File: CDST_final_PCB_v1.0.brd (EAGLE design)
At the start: 160 x 100 mm, 39 parts, among them IC1 MIC_I2S_SPH0645, U1 AD8232ACPZ-R7

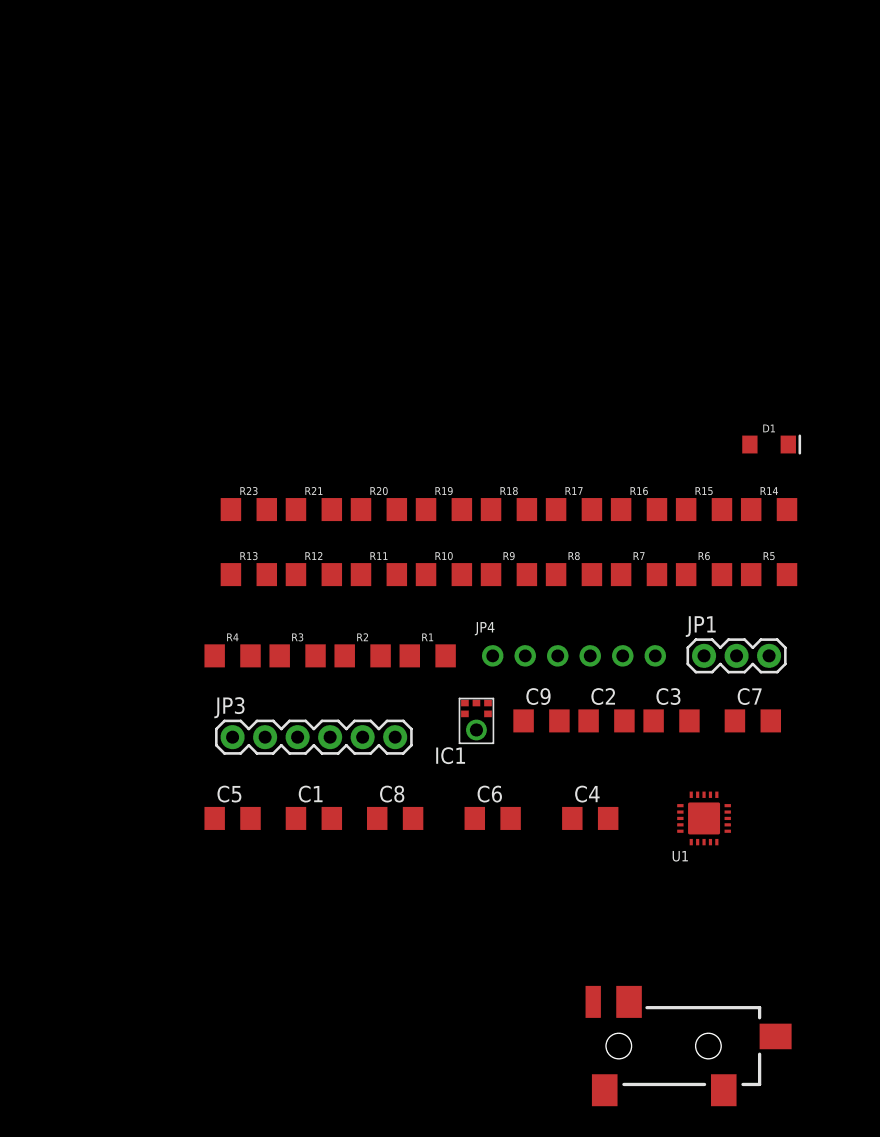
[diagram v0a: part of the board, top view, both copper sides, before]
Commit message: added power electronics
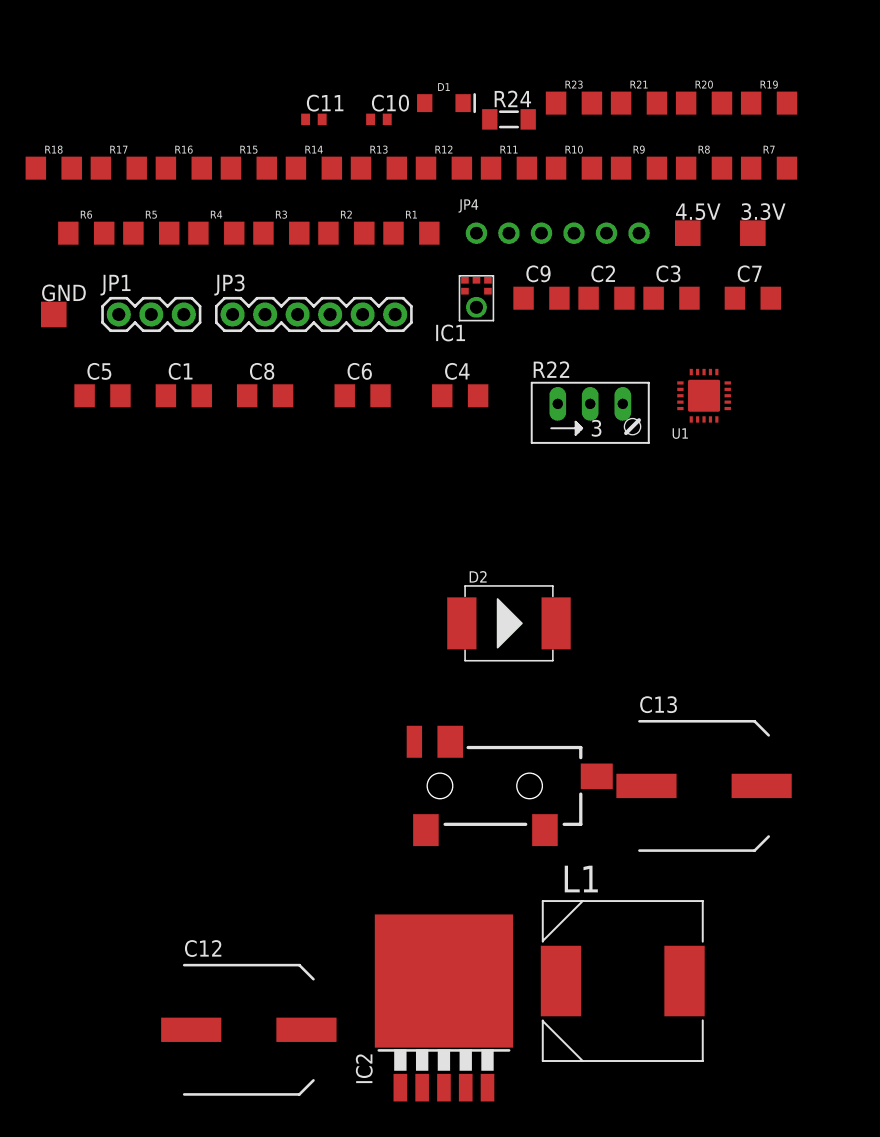
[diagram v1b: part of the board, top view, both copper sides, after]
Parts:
- added 3.3V, 4.5V, GND: TPTP20SQ, testpad:TP20SQ
- added C10, C11: (no value), rcl:C0402
- added C12, C13: (no value), rcl:SANYO-OSCON_SMD_F8
- added D2: SMD-DIODE-SCHOTTKY-40V-3A(DO-214AB), SMD-DIODE-SCHOTTKY-40V-3A_DO-214AB_:DO-214AB
- added IC2: LM2596S, national-semiconductor:TO263-5
- added L1: DR125-471-R, DR125-471-R:INDM125125X600N
- added R22: (no value), pot:RJ9W
- added R24: (no value), rcl:MINI_MELF-0204W
- moved R5 55.1 mm to (-63.5, 68.6)
- moved R6 55.1 mm to (-68.6, 68.6)
- moved JP1 52.9 mm to (-66.0, 62.2)
- moved R14 44.4 mm to (-50.8, 73.7)
- moved R15 44.4 mm to (-55.9, 73.7)
- moved R16 44.4 mm to (-61.0, 73.7)
- moved R17 44.4 mm to (-66.0, 73.7)
- moved R18 44.4 mm to (-71.1, 73.7)
- moved R23 40.7 mm to (-30.5, 78.7)
- moved R19 40.7 mm to (-15.2, 78.7)
- moved R20 40.7 mm to (-20.3, 78.7)
- moved R21 40.7 mm to (-25.4, 78.7)
- moved D1 36.8 mm to (-40.6, 78.7)
- moved C1 34.5 mm to (-61.0, 55.9)
- moved C5 34.5 mm to (-67.3, 55.9)
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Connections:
- new net N$12: C10.1, IC2.4, R22.E, R22.S, R24.2
- new net N$21: D2.2, IC2.2, L1.2
- new net N$6: 4.5V.TP, C11.1, C12.+, IC2.1
- new net V_REG: 3.3V.TP, C10.2, C13.+, C8.2, C9.2, JP4.1, L1.1, R17.1, R22.A
- net GND: now also C11.2, C12.-, C13.-, D2.1, GND.TP, IC2.3, IC2.5, R24.1
- net VCC: no longer R17.1
- net VDD: no longer C8.2, C9.2, JP4.1

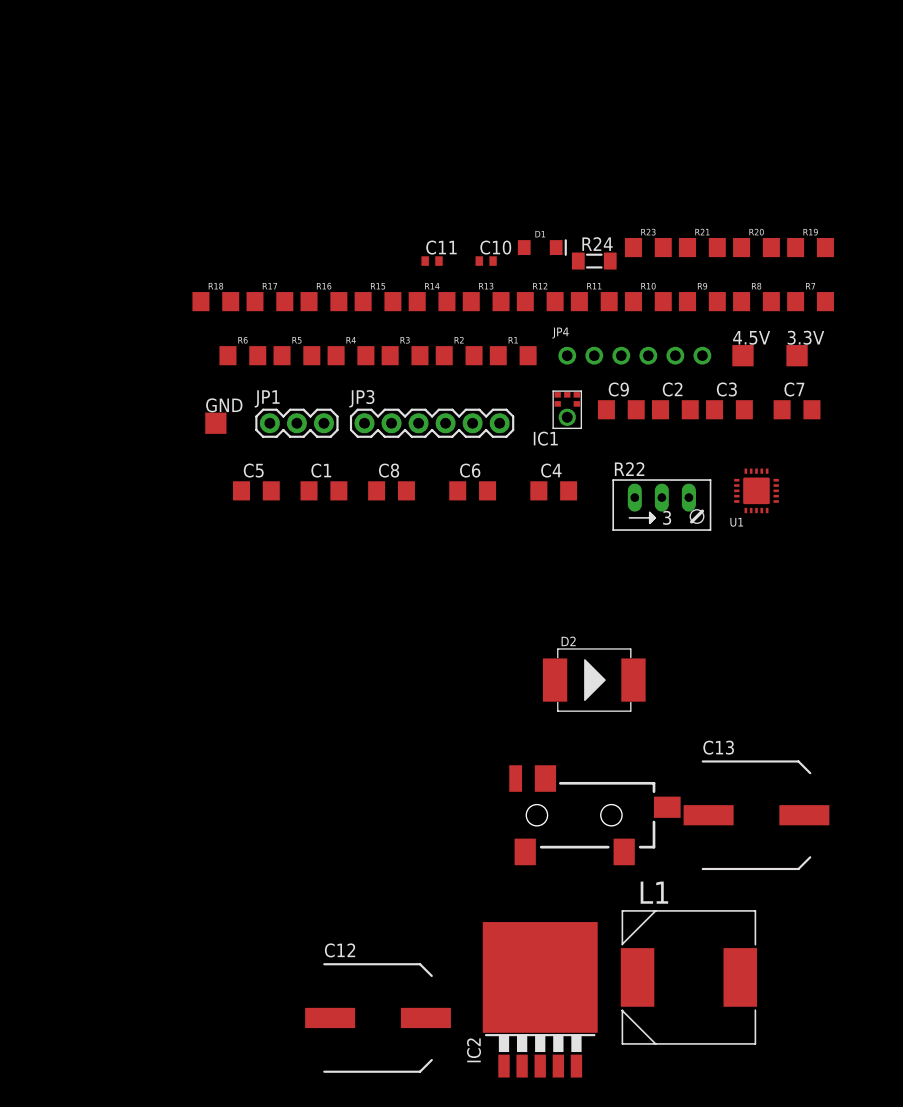
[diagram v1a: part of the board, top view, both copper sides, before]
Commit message: added esp32
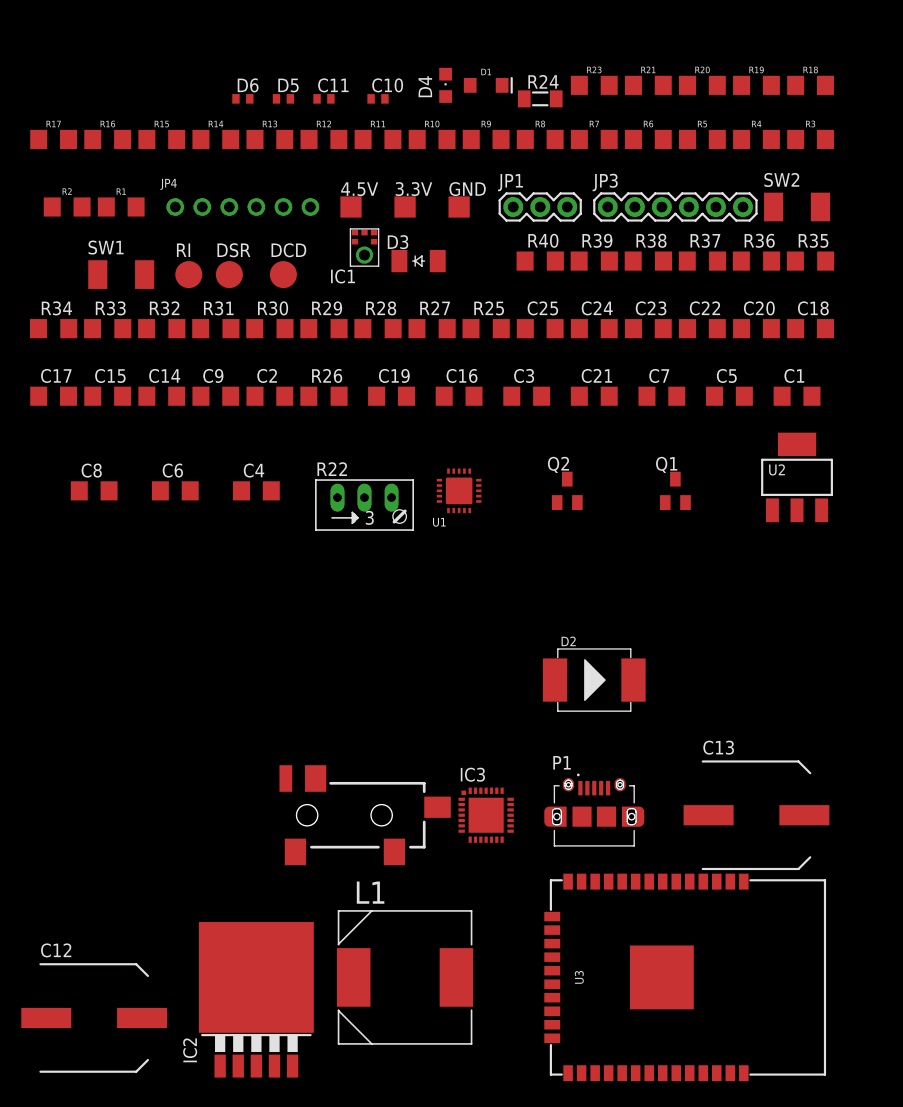
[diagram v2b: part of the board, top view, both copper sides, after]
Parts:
- added C14, C18, C20, C23: 10u, eagle-ltspice:C1206
- added C15: 22u, eagle-ltspice:C1206
- added C16, C19: 0.1u, eagle-ltspice:C1206
- added C17, C24, C25: 1n, eagle-ltspice:C1206
- added C21: 100u, eagle-ltspice:C1206
- added C22: 1u, eagle-ltspice:C1206
- added D3: CGRM4001-G, diode:SOD-123_MINI-SMA
- added D4: (no value), led:CHIPLED_0805
- added D5, D6: (no value), eagle-ltspice:R0402
- added DCD, DSR, RI: TPB2,54, testpad:B2,54
- added IC3: CP2101, silabs:MLP28
- added P1: ZX62D-B-5P8, ZX62D-B-5P8:HRS_ZX62D-B-5P8
- added Q1, Q2: BCX70SMD, transistor:SOT23
- added R25: 2k, eagle-ltspice:R1206
- added R26: 3.3k, eagle-ltspice:R1206
- added R27, R34, R35, R36, R37, R40: 0, eagle-ltspice:R1206
- added R28, R30, R31: 12k, eagle-ltspice:R1206
- added R29, R32, R33: 470, eagle-ltspice:R1206
- added R38, R39: 5k, eagle-ltspice:R1206
- added SW1, SW2: (no value), eagle-ltspice:R2010
- added U2: (no value), bt_regulator:SOT-223-3
- added U3: ESP-WROOM-03, esp32:ESP-WROOM-03
- moved R18 59.5 mm to (-15.2, 94.0)
- moved C1 45.3 mm to (-16.5, 64.8)
- moved C5 45.3 mm to (-22.9, 64.8)
- moved R3 43.2 mm to (-15.2, 88.9)
- moved R4 43.2 mm to (-20.3, 88.9)
- moved R5 43.2 mm to (-25.4, 88.9)
- moved R6 43.2 mm to (-30.5, 88.9)
- moved R1 39.4 mm to (-80.0, 82.5)
- moved R2 39.4 mm to (-85.1, 82.5)
- moved 3.3V 39.4 mm to (-53.3, 82.5)
- moved 4.5V 39.4 mm to (-58.4, 82.5)
- moved JP4 39.4 mm to (-68.6, 82.5)
- moved C2 38.1 mm to (-66.0, 64.8)
- moved C9 38.1 mm to (-71.1, 64.8)
- moved GND 30.6 mm to (-48.3, 82.5)
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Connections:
- removed net 3.3V: JP3.2, R15.2
- removed net VCC: C5.2, R10.1, R20.1, U1.15, U1.17
- removed net VDD: IC1.5
- new net DCD: DCD.TP, IC3.1
- new net HEATSINK: R40.2, U2.4
- new net N$20: C14.1, C16.1, C18.1, D3.C, IC3.8, R25.2, U2.3
- new net N$23: D5.2, IC3.4, P1.3
- new net N$24: D6.2, IC3.5, P1.2
- new net N$25: D3.A, P1.1
- new net N$26: Q1.1, R28.2
- new net N$27: IC3.24, Q1.2, R30.1, R36.2
- new net N$28: IC3.28, Q2.2, R28.1
- new net N$29: C24.1, Q1.3, R31.2, R33.2, U3.3
- new net N$30: IC3.25, R34.2
- new net N$31: IC3.26, R29.1
- new net N$33: U3.32, U3.37
- new net N$34: C25.1, R33.1, SW2.2
- new net N$35: C17.1, R32.1, SW1.2
- new net N$36: Q2.3, R32.2, R39.1, U3.25
- new net N$37: R38.2, U3.24
- new net N$38: R34.1, U3.35
- new net N$39: R29.2, R35.2
- new net N$40: R35.1, U3.34
- new net N$41: R36.1, U3.16
- new net N$42: IC3.23, R37.2
- new net N$43: R37.1, U3.23
- new net N$44: Q2.1, R30.2
- new net N$45: IC3.2, RI.TP
- new net N$46: DSR.TP, IC3.27
- net GND: now also C14.2, C15.2, C16.2, C17.2, C18.2, C19.2, C20.2, C21.2, C22.2, C23.1, C23.2, C24.2, C25.2, D4.C, D5.1, D6.1, IC3.3, IC3.EXP, IC3.M, P1.5, R26.1, R27.1, R27.2, R38.1, SW1.1, SW2.1, U2.1, U3.1, U3.15, U3.38, U3.GND
- net N$9: now also D4.A, R25.1; no longer C3.2, R8.2, U1.8
- net REFOUT: now also C3.2, R8.2, U1.8
- net V_REG: now also C15.1, C19.1, C20.1, C21.1, C22.1, C5.2, IC1.5, IC3.6, IC3.7, JP3.2, R10.1, R15.2, R20.1, R26.2, R31.1, R39.2, R40.1, U1.15, U1.17, U2.2, U3.2

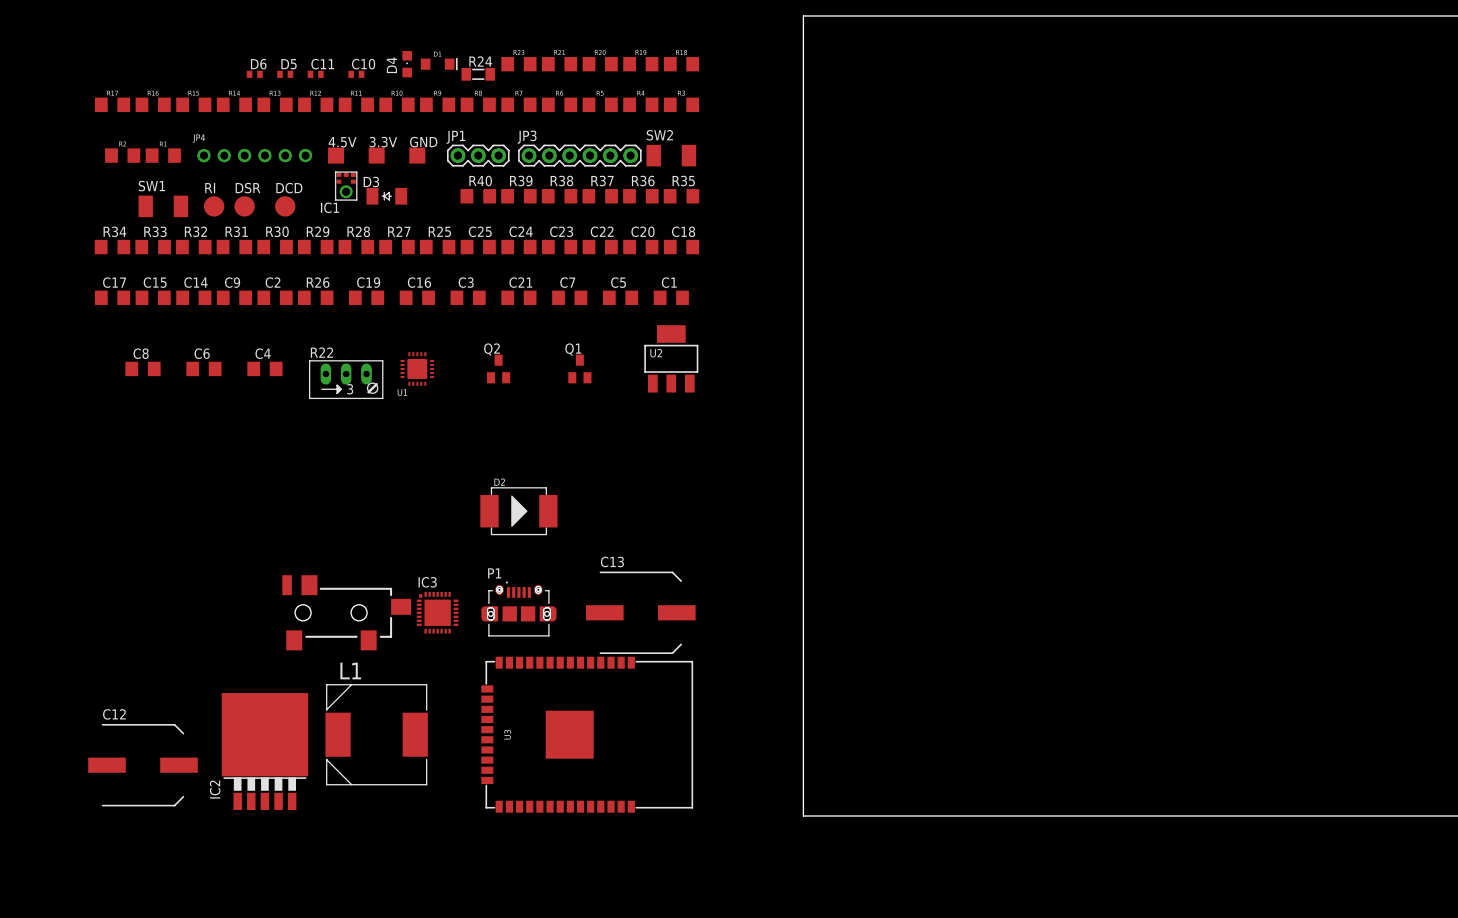
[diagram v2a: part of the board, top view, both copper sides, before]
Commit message: Test pin added to ESP
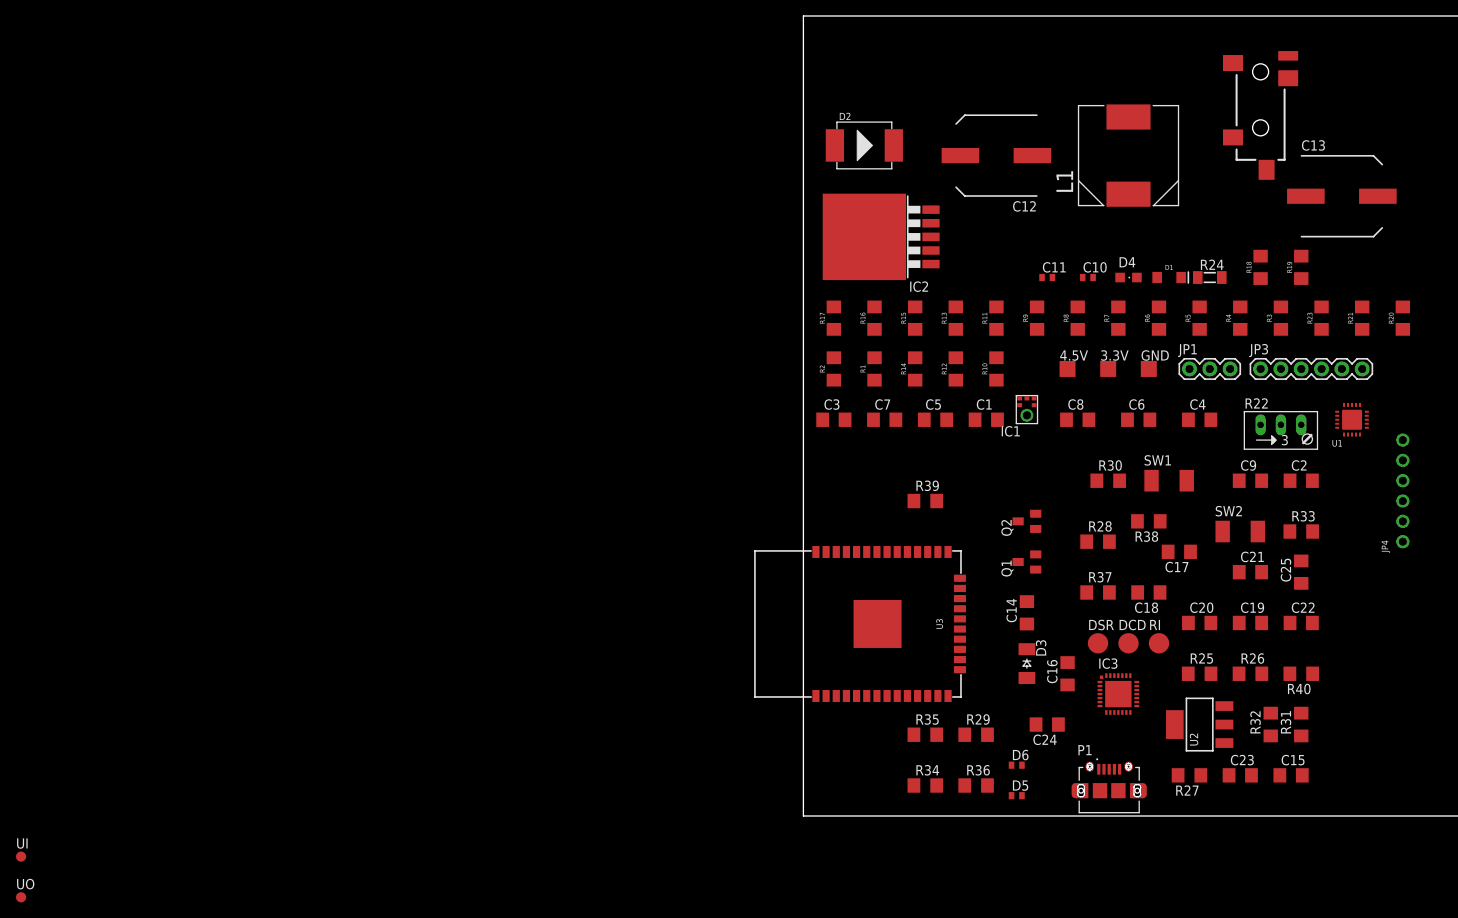
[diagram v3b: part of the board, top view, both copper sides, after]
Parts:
- added UI, UO: TPB1,27, testpad:B1,27
- moved C15 154.3 mm to (61.0, 5.08)
- moved JP4 149.5 mm to (74.9, 40.6), turned to 90 degrees
- moved R33 147.9 mm to (62.2, 35.6)
- moved R32 147.3 mm to (58.4, 11.4), turned to 90 degrees
- moved R31 146.1 mm to (62.2, 11.4), turned to 90 degrees
- moved JP2 142.2 mm to (57.1, 96.5), turned to 270 degrees
- moved C17 137.1 mm to (47.0, 33.0), turned to 180 degrees
- moved C12 131.1 mm to (24.1, 82.5), turned to 180 degrees
- moved SW1 130.3 mm to (45.7, 41.9)
- moved C2 130.3 mm to (62.2, 41.9)
- moved RI 130.1 mm to (44.5, 21.6)
- moved C9 129.0 mm to (55.9, 41.9)
- moved D6 128.6 mm to (26.7, 6.35)
- moved D5 128.4 mm to (26.7, 2.54)
- moved R26 125.9 mm to (55.9, 17.8)
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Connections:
- new net N$32: U3.13, UO.TP
- net BCLK: now also U3.11
- net DATA: now also R36.1, U3.16
- net GND: now also JP4.6
- net N$41: now also U3.14, UI.TP; no longer R36.1, U3.16
- net SELECT: no longer JP4.6
- net SIGNAL_OUT: now also U3.6
- net WS: now also U3.10

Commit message: layout revision v0.1
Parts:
- added D7: RED, SparkFun-LED:LED-1206
- added R41: 10k, SparkFun-Resistors:1206
- added S1: (no value), SparkFun-Switches:SWITCH_SPST_SMD_A
- added U4: 74LVC1G08SE, SparkFun-IC-Logic:SOT23-5
- moved UI 117.5 mm to (19.1, 7.62)
- moved UO 115.7 mm to (16.5, 7.62)
- moved FRAME1 109.8 mm to (15.2, -10.2)
- moved C3 52.2 mm to (53.3, 66.0), turned to 90 degrees
- moved R13 50.9 mm to (69.8, 64.8)
- moved JP1 47.9 mm to (66.0, 100.3), turned to 180 degrees
- moved R15 45.9 mm to (58.4, 73.7), turned to 180 degrees
- moved R17 43.0 mm to (44.5, 76.2), turned to 270 degrees
- moved R34 41.0 mm to (3.81, 43.2)
- moved R11 40.7 mm to (64.8, 63.5)
- moved 4.5V 39.6 mm to (29.2, 95.2), flipped to the bottom
- moved R22 38.6 mm to (33.0, 76.2)
- moved GND 37.0 mm to (29.2, 90.2), flipped to the bottom
- moved R24 34.9 mm to (39.4, 100.3), turned to 180 degrees
- moved R18 34.3 mm to (22.9, 67.3), turned to 270 degrees
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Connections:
- new net N$47: D7.A, S1.1
- new net N$48: R21.2, U4.2
- new net N$49: R41.1, S1.2, U4.1
- net DATA: now also U4.4; no longer R21.2
- net GND: now also D7.C, U4.3
- net V_REG: now also R41.2, U4.5
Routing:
- net GND: track 0.00 -> 670.2 mm, vias 0 -> 7
- net V_REG: track 0.00 -> 438.3 mm, vias 0 -> 9
- net SIGNAL_OUT: track 0.00 -> 164.9 mm, vias 0 -> 2
- net LA: track 0.00 -> 113.0 mm, vias 0 -> 3
- net N$36: track 0.00 -> 107.7 mm
- net N$29: track 0.00 -> 106.4 mm, vias 0 -> 5
- net DATA: track 0.00 -> 105.1 mm, vias 0 -> 2
- net N$9: track 0.00 -> 102.3 mm
- net RA: track 0.00 -> 94.9 mm, vias 0 -> 1
- net N$20: track 0.00 -> 91.8 mm, vias 0 -> 6
- net N$8: track 0.00 -> 91.6 mm, vias 0 -> 3
- net WS: track 0.00 -> 90.2 mm, vias 0 -> 2
- net BCLK: track 0.00 -> 89.6 mm, vias 0 -> 2
- net N$48: track 0.00 -> 78.2 mm, vias 0 -> 2
- net N$3: track 0.00 -> 74.8 mm
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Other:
- board size 160 x 100 mm -> 82.5 x 103.8 mm
